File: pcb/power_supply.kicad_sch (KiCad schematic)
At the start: 30 parts, among them CN1 VL0631510000G, U5 AOZ1284PI

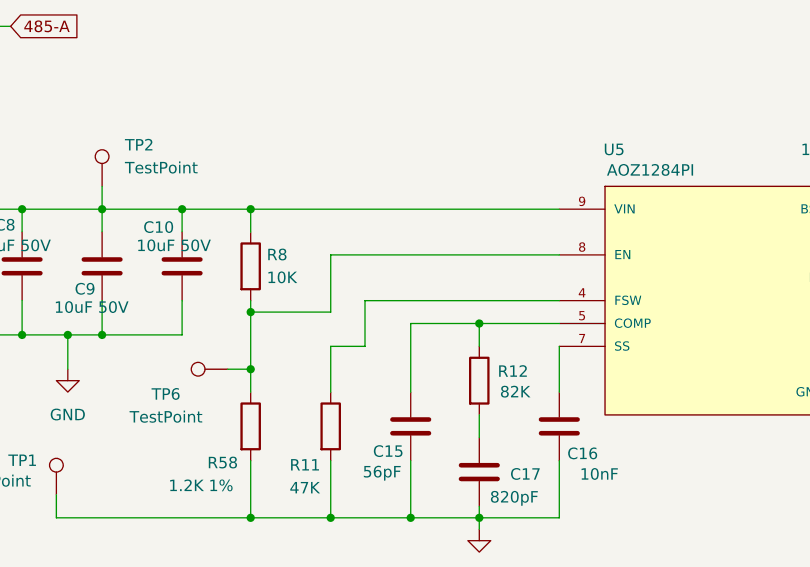
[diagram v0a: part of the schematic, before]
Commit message: Updated pcb and sent to prototype production as the first official version.
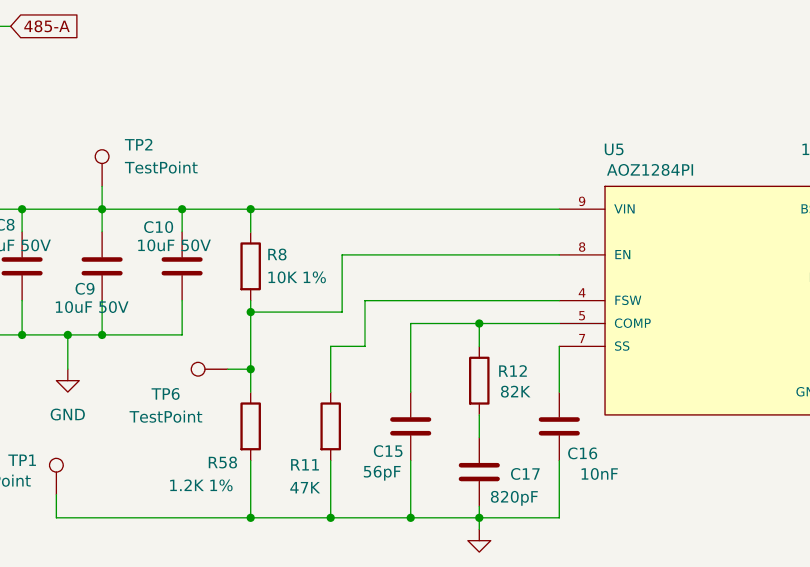
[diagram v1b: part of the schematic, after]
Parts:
- R59: footprint Resistor_SMD:R_0815_2038Metric_Pad1.20x4.05mm_HandSolder -> Resistor_SMD:R_1206_3216Metric_Pad1.30x1.75mm_HandSolder
- R8: value 10K -> 10K 1%
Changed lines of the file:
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@@
 	(wire
 		(pts
-			(xy 111.76 109.22) (xy 120.65 109.22)
+			(xy 111.76 109.22) (xy 121.92 109.22)
 		)
 		(stroke
@@
 	(wire
 		(pts
-			(xy 120.65 109.22) (xy 120.65 102.87)
+			(xy 121.92 109.22) (xy 121.92 102.87)
 		)
 		(stroke
@@
 	(wire
 		(pts
-			(xy 120.65 102.87) (xy 146.05 102.87)
+			(xy 121.92 102.87) (xy 146.05 102.87)
 		)
 		(stroke
@@
 			)
 		)
-		(property "Value" "10K"
+		(property "Value" "10K 1%"
 			(at 113.538 105.41 0)
 			(effects
@@
 			)
 		)
-		(property "Footprint" "Resistor_SMD:R_0815_2038Metric_Pad1.20x4.05mm_HandSolder"
+		(property "Footprint" "Resistor_SMD:R_1206_3216Metric_Pad1.30x1.75mm_HandSolder"
 			(at 195.58 74.168 90)
 			(effects
